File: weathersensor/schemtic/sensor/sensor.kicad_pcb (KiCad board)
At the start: 2 copper layers, 151 x 81 mm, 12 parts, among them J1 Conn_Coaxial, J2 MS5611, J3 MS5611, J4 PANEL, J7 BAT, U1 LoRa-E5, U2 RFM95W-868S2, U4 TSR_1-2450, U5 INA226

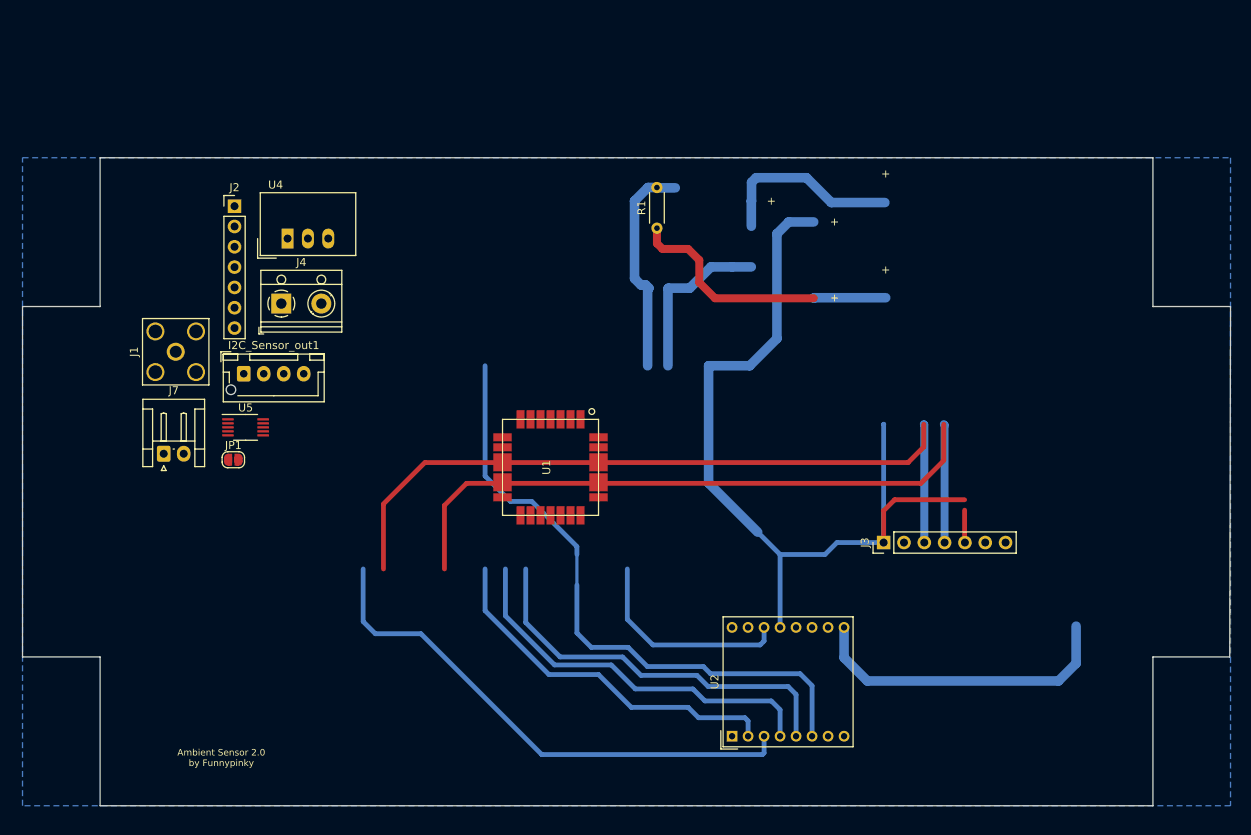
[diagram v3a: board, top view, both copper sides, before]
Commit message: Änderung des Sensor auf neue Plattform STM32WLxx Lora-e5
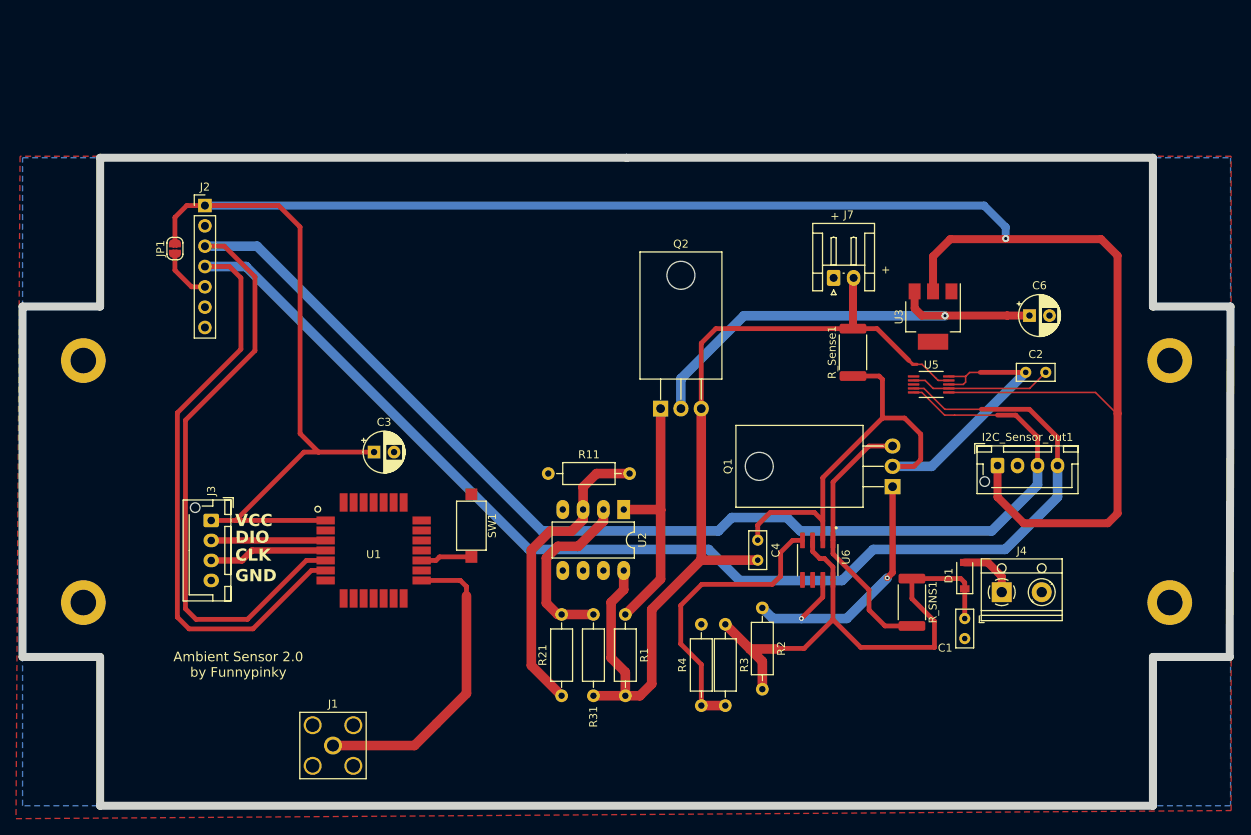
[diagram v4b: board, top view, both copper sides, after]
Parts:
- removed U4: TSR_1-2450, Converter_DCDC:Converter_DCDC_TRACO_TSR-1_THT
- added C1: 0.1uF, Capacitor_THT:C_Rect_L4.6mm_W2.0mm_P2.50mm_MKS02_FKP02, F.Cu at (168.4, 90.3)
- added C2: 0.1uF, Capacitor_THT:C_Rect_L4.6mm_W2.0mm_P2.50mm_MKS02_FKP02, F.Cu at (176.0, 59.5)
- added C3: 100u/25V, Capacitor_THT:CP_Radial_D5.0mm_P2.50mm, F.Cu at (94.5, 69.5)
- added C4: 0.1uF, Capacitor_THT:C_Rect_L4.6mm_W2.0mm_P2.50mm_MKS02_FKP02, F.Cu at (142.5, 80.5)
- added C6: 100u/25V, Capacitor_THT:CP_Radial_D5.0mm_P2.50mm, F.Cu at (176.5, 52.4)
- added D1: D_Schottky, Diode_SMD:D_SOD-123, F.Cu at (168.4, 84.9)
- added Q1: IRF9540N, Package_TO_SOT_THT:TO-220-3_Horizontal_TabDown, F.Cu at (159.4, 73.8)
- added Q2: IRF9540N, Package_TO_SOT_THT:TO-220-3_Horizontal_TabDown, F.Cu at (130.4, 64.1)
- added R11: 1.3M, Resistor_THT:R_Axial_DIN0207_L6.3mm_D2.5mm_P10.16mm_Horizontal, F.Cu at (116.3, 72.2)
- added R2: 1k, Resistor_THT:R_Axial_DIN0207_L6.3mm_D2.5mm_P10.16mm_Horizontal, F.Cu at (143.1, 89.0)
- added R21: 1.7M, Resistor_THT:R_Axial_DIN0207_L6.3mm_D2.5mm_P10.16mm_Horizontal, F.Cu at (118.0, 100.0)
- added R3: 10k, Resistor_THT:R_Axial_DIN0207_L6.3mm_D2.5mm_P10.16mm_Horizontal, F.Cu at (138.4, 101.2)
- added R31: 300k, Resistor_THT:R_Axial_DIN0207_L6.3mm_D2.5mm_P10.16mm_Horizontal, F.Cu at (122.0, 89.8)
- added R4: 10k, Resistor_THT:R_Axial_DIN0207_L6.3mm_D2.5mm_P10.16mm_Horizontal, F.Cu at (135.4, 101.2)
- added REF**: MountingHole_3.2mm_M3_DIN965_Pad, MountingHole:MountingHole_3.2mm_M3_DIN965_Pad, F.Cu at (194.0, 58.0)
- added REF**: MountingHole_3.2mm_M3_DIN965_Pad, MountingHole:MountingHole_3.2mm_M3_DIN965_Pad, F.Cu at (58.2, 88.3)
- added REF**: MountingHole_3.2mm_M3_DIN965_Pad, MountingHole:MountingHole_3.2mm_M3_DIN965_Pad, F.Cu at (194.0, 88.3)
- added REF**: MountingHole_3.2mm_M3_DIN965_Pad, MountingHole:MountingHole_3.2mm_M3_DIN965_Pad, F.Cu at (58.2, 58.0)
- added R_SNS1: 0.05, Resistor_SMD:R_2512_6332Metric, F.Cu at (161.8, 88.3)
- added R_Sense1: 0.025, Resistor_SMD:R_2512_6332Metric, F.Cu at (154.4, 57.0)
- added SW1: SW_Push, Button_Switch_SMD:SW_SPST_CK_RS282G05A3, F.Cu at (106.7, 78.7)
- added U3: AZ1117-3.3, Package_TO_SOT_SMD:SOT-223, F.Cu at (164.4, 52.6)
- added U6: BQ2057WSN, BQ2057WSN:SOIC127P599X175-8N, F.Cu at (150.0, 83.0)
- J3: value MS5611 -> SWD; footprint Connector_PinHeader_2.54mm:PinHeader_1x07_P2.54mm_Vertical -> Connector_JST:JST_XH_B4B-XH-AM_1x04_P2.50mm_Vertical
- R1: value 10M -> 10k; footprint Resistor_THT:R_Axial_DIN0204_L3.6mm_D1.6mm_P5.08mm_Horizontal -> Resistor_THT:R_Axial_DIN0207_L6.3mm_D2.5mm_P10.16mm_Horizontal
- U2: value RFM95W-868S2 -> ICL7665; footprint RF_Module:HOPERF_RFM9XW_THT -> Package_DIP:DIP-8_W7.62mm_LongPads
- moved J4 97.0 mm to (173.0, 87.0)
- moved I2C_Sensor_out1 94.9 mm to (172.5, 71.2)
- moved J7 86.6 mm to (152.0, 47.7)
- moved U5 85.9 mm to (164.2, 61.0)
- moved J3 84.1 mm to (74.2, 78.0), turned to -90 degrees
- moved J1 53.0 mm to (89.4, 106.2), turned to -90 degrees
- moved R1 48.5 mm to (126.0, 89.8), turned to -90 degrees
- moved U2 31.4 mm to (125.8, 76.7), turned to -90 degrees
- moved JP1 27.4 mm to (69.7, 44.0), turned to 90 degrees
- moved U1 24.4 mm to (94.5, 81.8), turned to 0 degrees
- moved J2 3.70 mm to (73.4, 38.7)
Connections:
- I2C_Sensor_out1 pad 2: GND -> BAT-
- J1 pad 2: GND -> BAT-
- J2 pad 2: GND -> BAT-
- J3 pad 2: GND -> SWDIO
- J3 pad 3: SCL -> SWCLK
- J3 pad 4: SDA -> BAT-
- J4 pad 2: GND -> BAT-
- J7 pad 1: GND -> BAT-
- J7 pad 2: BAT -> BAT+
- R1 pad 1: Net-(J4-Pad1) -> Net-(Q2-G)
- R1 pad 2: V_PANEL -> BAT+
- U1 pad 14: GND -> BAT-
- U1 pad 16: GND -> BAT-
- U1 pad 2: GND -> BAT-
- U1 pad 22: GND -> BAT-
- U1 pad 5: unconnected-(U1-PB15-Pad5) -> SCL
- U1 pad 6: unconnected-(U1-PA15-Pad6) -> SDA
- U2 pad 1: GND -> Net-(Q2-G)
- U2 pad 2: MISO -> Net-(U2-HYST1)
- U2 pad 3: MOSI -> Net-(U2-SET1)
- U2 pad 4: CLK -> BAT-
- U2 pad 5: NSS -> unconnected-(U2-HYST2-Pad5)
- U2 pad 6: Net-(U1-Pad12) -> unconnected-(U2-SET2-Pad6)
- U2 pad 8: GND -> BAT+
- U5 pad 1: unconnected-(U5-A1-Pad1) -> BAT-
- U5 pad 10: Net-(U2-BAT-) -> VIN+
- U5 pad 2: unconnected-(U5-A0-Pad2) -> BAT-
- U5 pad 4: unconnected-(U5-SDA-Pad4) -> SDA
- U5 pad 5: unconnected-(U5-SCL-Pad5) -> SCL
- U5 pad 7: GND -> BAT-
- U5 pad 8: BAT -> VIN+
- U5 pad 9: GND -> BAT+
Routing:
- net VCC: track 107.7 -> 291.9 mm, vias 0 -> 1
- net SDA: track 92.1 -> 228.1 mm
- net SCL: track 96.3 -> 220.5 mm
- net BAT+: track 0.00 -> 118.0 mm
- net VIN+: track 0.00 -> 85.1 mm
- net Net-(U1-Pad12): track 78.2 -> 0.00 mm
- net Net-(D1-K): track 0.00 -> 68.4 mm
- net MOSI: track 65.8 -> 0.00 mm
- net Net-(Q2-D): track 0.00 -> 56.9 mm, vias 0 -> 1
- net NSS: track 49.4 -> 0.00 mm
- net CLK: track 48.4 -> 0.00 mm
- net MISO: track 45.7 -> 0.00 mm
- net Net-(J1-Pad1): track 39.6 -> 0.00 mm
- net RFIO: track 0.00 -> 38.7 mm
- net Net-(U2-SET1): track 0.00 -> 38.4 mm
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- added copper zone on B.Cu, net BAT-
- added copper zone on F.Cu, net BAT-
- removed copper zone on B.Cu, net GND
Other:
- board text added: "CLK"
- board text added: "DIO"
- board text added: "GND"
- board text added: "VCC"
